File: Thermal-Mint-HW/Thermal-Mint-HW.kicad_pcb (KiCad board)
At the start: 4 copper layers, 90 x 54 mm, 36 parts, among them J1 Molex_5031821852, U1 ADS1220-VQFN, U2 ADS1220-VQFN, U3 ESP32-C3

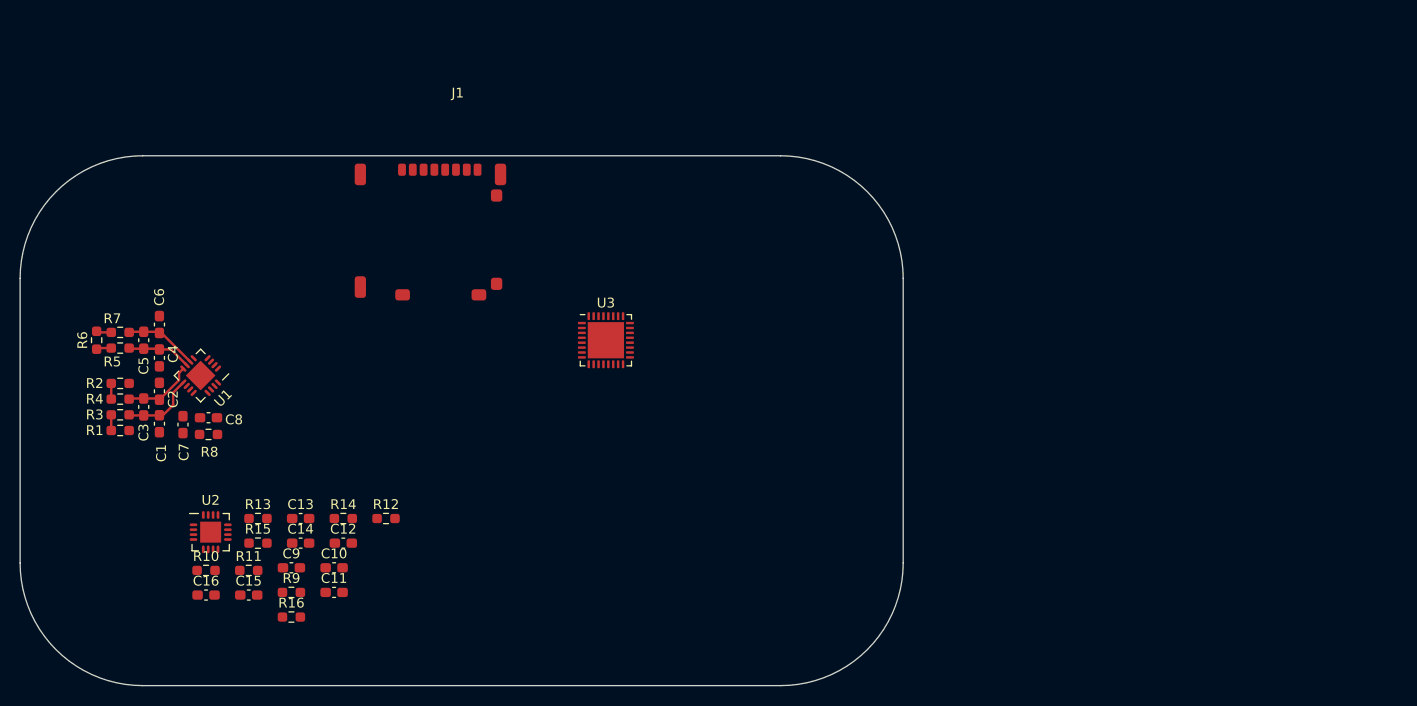
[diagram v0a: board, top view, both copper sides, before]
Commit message: WIP commit, Adding connectors and memory
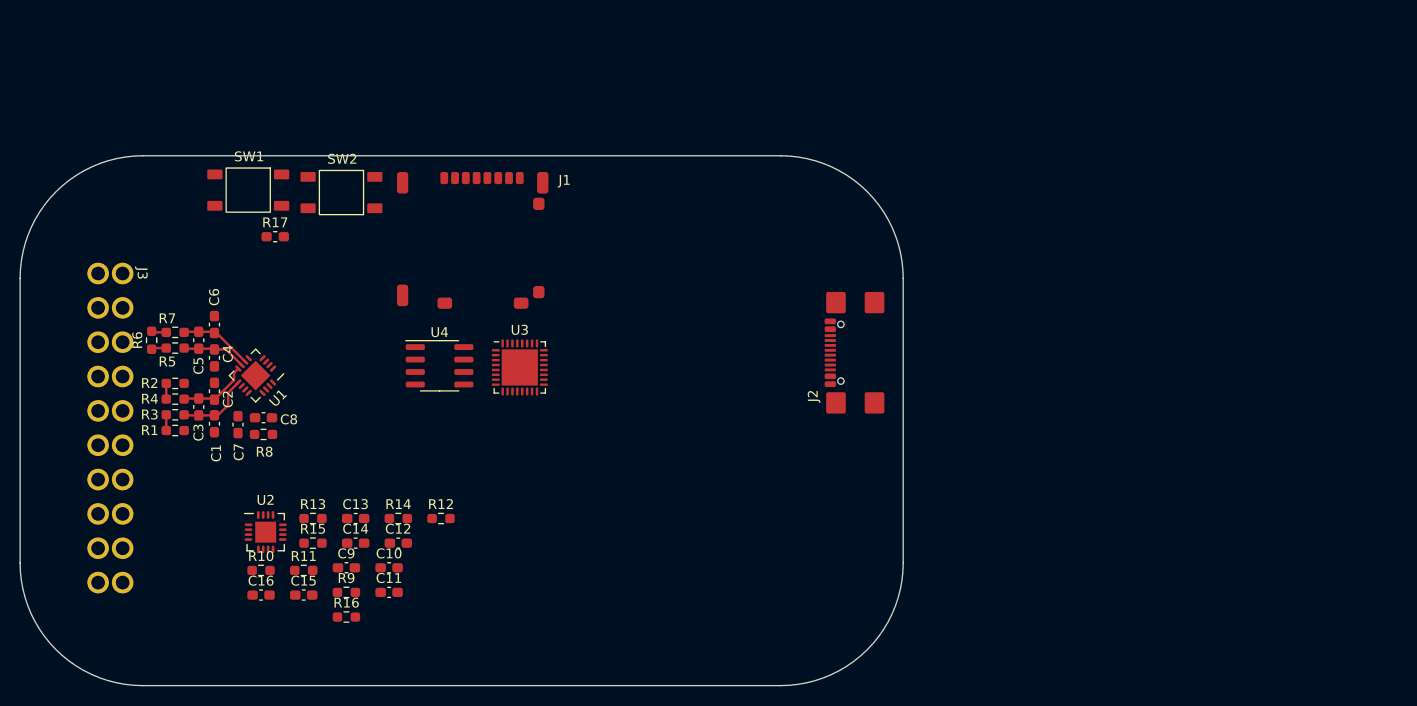
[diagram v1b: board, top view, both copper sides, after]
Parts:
- added J2: USB_C_Receptacle_USB2.0, ThermalMint:USB4110-GF-A, F.Cu at (144.6, 80.1)
- added J3: Conn_01x20_Male, ThermalMint:1786918_02_DMC, F.Cu at (72.5, 72.0)
- added R17: R, Resistor_SMD:R_0603_1608Metric_Pad1.05x0.95mm_HandSolder, F.Cu at (88.0, 68.2)
- added SW1: SW_SPST, ThermalMint:SW_SPST_PTS647, F.Cu at (85.2, 63.5)
- added SW2: SW_SPST, ThermalMint:SW_SPST_PTS647, F.Cu at (94.8, 63.8)
- added U4: AT25DL081-SSHN-T, Package_SO:SOIC-8_3.9x4.9mm_P1.27mm, F.Cu at (104.8, 81.4)
- J1: footprint CH:Molex_SDCard_5031821852 -> ThermalMint:Molex_SDCard_5031821852
- moved U3 9.20 mm to (112.9, 81.6)
- moved C10 5.61 mm to (99.6, 102.0)
- moved C11 5.61 mm to (99.6, 104.5)
- moved C12 5.61 mm to (100.5, 99.5)
- moved C15 5.61 mm to (90.9, 104.8)
- moved C3 5.61 mm to (80.2, 85.6)
- moved C5 5.61 mm to (80.2, 78.8)
- moved C7 5.61 mm to (84.2, 87.4)
- moved R11 5.61 mm to (90.9, 102.3)
- moved R13 5.61 mm to (91.8, 97.0)
- moved R14 5.61 mm to (100.5, 97.0)
- moved R15 5.61 mm to (91.8, 99.5)
- moved R6 5.61 mm to (75.4, 78.8)
- moved U2 5.61 mm to (87.0, 98.4)
- moved C1 5.61 mm to (81.8, 87.3)
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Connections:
- net /ADS1220_1/AIN0 renamed /ADC1AIN0
- net /ADS1220_1/AIN1 renamed /ADC1AIN1
- net /ADS1220_1/AIN2 renamed /ADC1AIN2
- net /ADS1220_1/RefIn renamed /ADC1REFIN
- net /ADS1220_1/nDRDY renamed Net-(R19-Pad1)
- net /ADS1220_2/AIN0 renamed /ADC2AIN0
- net /ADS1220_2/AIN1 renamed /ADC2AIN1
- net /ADS1220_2/RefIn renamed /ADC2REFIN
- net /ADS1220_2/nDRDY renamed Net-(R21-Pad1)
- net CS renamed /TM-ESP32/CS3
- net MISO renamed Net-(J1-Pad7)
- net RXD renamed /TM-ESP32/RXD
- net TXD renamed /TM-ESP32/TXD
- C16 pad 1: 3V3 -> +3V3
- C8 pad 1: 3V3 -> +3V3
- J1 pad 3: MOSI -> /ADS1220_1/DIN
- J1 pad 5: CLK -> /ADS1220_1/SCLK
- J1 pad 9: unconnected-(J1-Pad9) -> /TM-SDCard/cardDetect
- R16 pad 2: 3V3 -> +3V3
- R8 pad 2: 3V3 -> +3V3
- U1 pad 11: 3V3 -> +3V3
- U1 pad 13: /ADS1220_1/DOUT -> Net-(R18-Pad1)
- U1 pad 4: /ADS1220_1/AIN3 -> /ADC1AIN3
- U2 pad 11: 3V3 -> +3V3
- U2 pad 13: /ADS1220_1/DOUT -> Net-(R20-Pad1)
- U2 pad 4: /ADS1220_2/AIN3 -> /ADC3AIN3
- U2 pad 5: /ADS1220_2/AIN2 -> /ADC2AIN3
- U3 pad 1: unconnected-(U3-Pad1) -> /TM-ESP32/RF
- U3 pad 25: D- -> /TM-ESP32/D-
- U3 pad 26: D+ -> /TM-ESP32/D+
- U3 pad 33: unconnected-(U3-Pad33) -> GND

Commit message: Clean up of output circuits
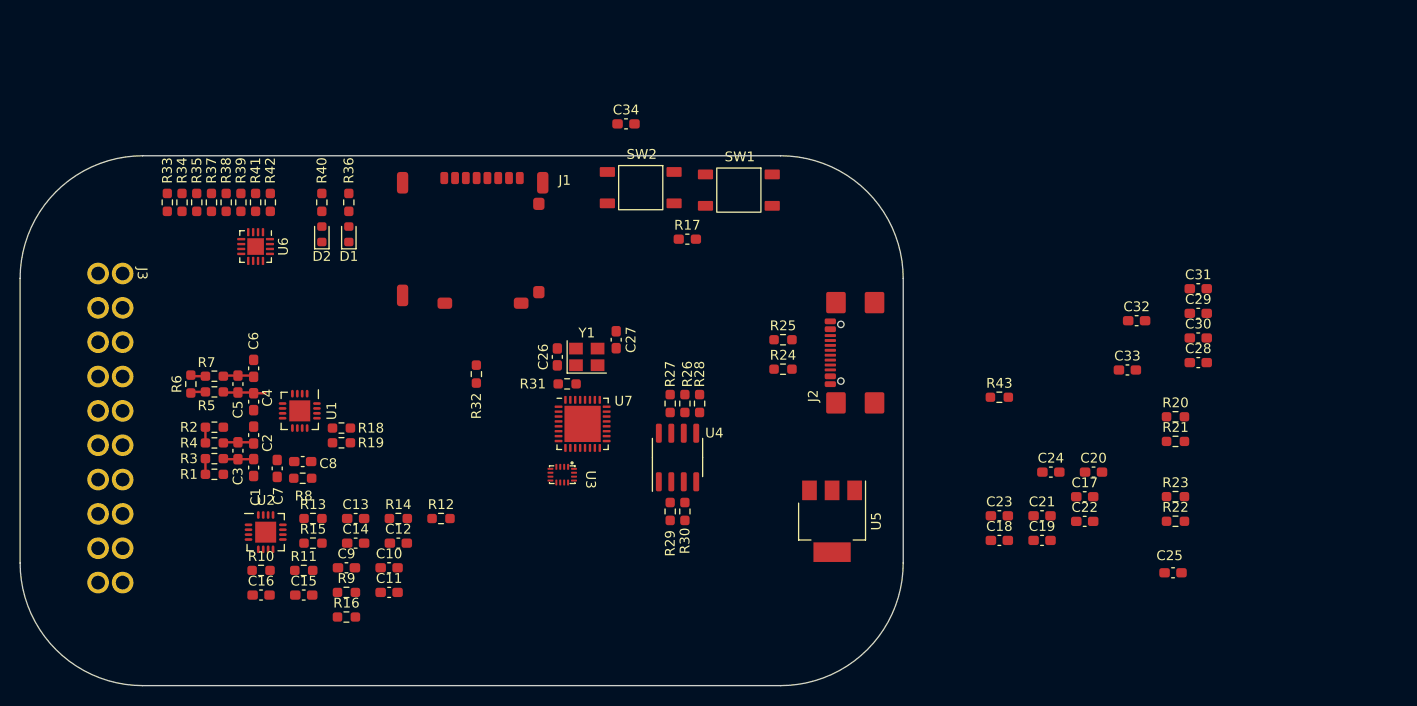
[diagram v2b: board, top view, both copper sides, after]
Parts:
- added C17: 470n, Capacitor_SMD:C_0603_1608Metric_Pad1.08x0.95mm_HandSolder, F.Cu at (170.5, 94.8)
- added C18: 470n, Capacitor_SMD:C_0603_1608Metric_Pad1.08x0.95mm_HandSolder, F.Cu at (161.8, 99.2)
- added C19: 470n, Capacitor_SMD:C_0603_1608Metric_Pad1.08x0.95mm_HandSolder, F.Cu at (166.2, 99.2)
- added C20: 470n, Capacitor_SMD:C_0603_1608Metric_Pad1.08x0.95mm_HandSolder, F.Cu at (171.4, 92.2)
- added C21: 470n, Capacitor_SMD:C_0603_1608Metric_Pad1.08x0.95mm_HandSolder, F.Cu at (166.2, 96.7)
- added C22: 470n, Capacitor_SMD:C_0603_1608Metric_Pad1.08x0.95mm_HandSolder, F.Cu at (170.5, 97.3)
- added C23: 470n, Capacitor_SMD:C_0603_1608Metric_Pad1.08x0.95mm_HandSolder, F.Cu at (161.8, 96.7)
- added C24: 470n, Capacitor_SMD:C_0603_1608Metric_Pad1.08x0.95mm_HandSolder, F.Cu at (167.1, 92.2)
- added C25: 470n, Capacitor_SMD:C_0603_1608Metric_Pad1.08x0.95mm_HandSolder, F.Cu at (179.5, 102.5)
- added C26: 15p, Capacitor_SMD:C_0603_1608Metric_Pad1.08x0.95mm_HandSolder, F.Cu at (116.8, 80.5)
- added C27: 15p, Capacitor_SMD:C_0603_1608Metric_Pad1.08x0.95mm_HandSolder, F.Cu at (122.8, 78.8)
- added C28: 470n, Capacitor_SMD:C_0603_1608Metric_Pad1.08x0.95mm_HandSolder, F.Cu at (182.1, 81.1)
- added C29: 470n, Capacitor_SMD:C_0603_1608Metric_Pad1.08x0.95mm_HandSolder, F.Cu at (182.1, 76.1)
- added C30: 470n, Capacitor_SMD:C_0603_1608Metric_Pad1.08x0.95mm_HandSolder, F.Cu at (182.1, 78.6)
- added C31: 470n, Capacitor_SMD:C_0603_1608Metric_Pad1.08x0.95mm_HandSolder, F.Cu at (182.1, 73.5)
- added C32: 470n, Capacitor_SMD:C_0603_1608Metric_Pad1.08x0.95mm_HandSolder, F.Cu at (175.8, 76.8)
- added C33: 470n, Capacitor_SMD:C_0603_1608Metric_Pad1.08x0.95mm_HandSolder, F.Cu at (174.8, 81.8)
- added C34: 470n, Capacitor_SMD:C_0603_1608Metric_Pad1.08x0.95mm_HandSolder, F.Cu at (123.8, 56.8)
- added D1: LED, LED_SMD:LED_0603_1608Metric, F.Cu at (95.5, 68.0)
- added D2: LED, LED_SMD:LED_0603_1608Metric, F.Cu at (92.8, 68.0)
- added R18: 24, Resistor_SMD:R_0603_1608Metric_Pad0.98x0.95mm_HandSolder, F.Cu at (94.8, 87.8)
- added R19: 24, Resistor_SMD:R_0603_1608Metric_Pad0.98x0.95mm_HandSolder, F.Cu at (94.8, 89.2)
- added R20: 24, Resistor_SMD:R_0603_1608Metric_Pad0.98x0.95mm_HandSolder, F.Cu at (179.8, 86.6)
- added R21: 24, Resistor_SMD:R_0603_1608Metric_Pad0.98x0.95mm_HandSolder, F.Cu at (179.8, 89.1)
- added R22: 24, Resistor_SMD:R_0603_1608Metric_Pad0.98x0.95mm_HandSolder, F.Cu at (179.8, 97.2)
- added R23: 10k, Resistor_SMD:R_0603_1608Metric_Pad0.98x0.95mm_HandSolder, F.Cu at (179.8, 94.7)
- added R24: 5.1k, Resistor_SMD:R_0603_1608Metric_Pad0.98x0.95mm_HandSolder, F.Cu at (139.8, 81.8)
- added R25: 5.1k, Resistor_SMD:R_0603_1608Metric_Pad0.98x0.95mm_HandSolder, F.Cu at (139.8, 78.8)
- added R26: R, Resistor_SMD:R_0603_1608Metric_Pad0.98x0.95mm_HandSolder, F.Cu at (129.8, 85.2)
- added R27: R, Resistor_SMD:R_0603_1608Metric_Pad0.98x0.95mm_HandSolder, F.Cu at (128.2, 85.2)
- added R28: R, Resistor_SMD:R_0603_1608Metric_Pad0.98x0.95mm_HandSolder, F.Cu at (131.2, 85.2)
- added R29: R, Resistor_SMD:R_0603_1608Metric_Pad0.98x0.95mm_HandSolder, F.Cu at (128.2, 96.2)
- added R30: R, Resistor_SMD:R_0603_1608Metric_Pad0.98x0.95mm_HandSolder, F.Cu at (129.8, 96.2)
- added R31: 0, Resistor_SMD:R_0603_1608Metric_Pad0.98x0.95mm_HandSolder, F.Cu at (117.8, 83.2)
- added R32: 10k, Resistor_SMD:R_0603_1608Metric_Pad0.98x0.95mm_HandSolder, F.Cu at (108.5, 82.2)
- added R33: 1k, Resistor_SMD:R_0603_1608Metric_Pad0.98x0.95mm_HandSolder, F.Cu at (77.0, 64.8)
- added R34: 1k, Resistor_SMD:R_0603_1608Metric_Pad0.98x0.95mm_HandSolder, F.Cu at (78.5, 64.8)
- added R35: 1k, Resistor_SMD:R_0603_1608Metric_Pad0.98x0.95mm_HandSolder, F.Cu at (80.0, 64.8)
- added R36: 1k, Resistor_SMD:R_0603_1608Metric_Pad0.98x0.95mm_HandSolder, F.Cu at (95.5, 64.8)
- added R37: 1k, Resistor_SMD:R_0603_1608Metric_Pad0.98x0.95mm_HandSolder, F.Cu at (81.5, 64.8)
- added R38: 1k, Resistor_SMD:R_0603_1608Metric_Pad0.98x0.95mm_HandSolder, F.Cu at (83.0, 64.8)
- added R39: 1k, Resistor_SMD:R_0603_1608Metric_Pad0.98x0.95mm_HandSolder, F.Cu at (84.5, 64.8)
- added R40: 1k, Resistor_SMD:R_0603_1608Metric_Pad0.98x0.95mm_HandSolder, F.Cu at (92.8, 64.8)
- added R41: 1k, Resistor_SMD:R_0603_1608Metric_Pad0.98x0.95mm_HandSolder, F.Cu at (86.0, 64.8)
- added R42: 1k, Resistor_SMD:R_0603_1608Metric_Pad0.98x0.95mm_HandSolder, F.Cu at (87.5, 64.8)
- added R43: 24, Resistor_SMD:R_0603_1608Metric_Pad0.98x0.95mm_HandSolder, F.Cu at (161.8, 84.6)
- added U3: SN74LVC138ARSVR, ThermalMint:UQFN16 - RSV0016A, F.Cu at (117.2, 92.5)
- added U5: NCP1117-3.3_SOT223, Package_TO_SOT_SMD:SOT-223-3_TabPin2, F.Cu at (144.8, 97.2)
- added U6: MAX7317ATE+, Package_DFN_QFN:QFN-16-1EP_3x3mm_P0.5mm_EP1.7x1.7mm, F.Cu at (86.0, 69.2)
- added Y1: FL4000157Z, Crystal:Crystal_SMD_3225-4Pin_3.2x2.5mm, F.Cu at (119.8, 80.5)
- J2: value USB_C_Receptacle_USB2.0 -> USB4110-GF-A
- R17: value R -> 10k
- SW1, SW2: value SW_SPST -> PTS647
- moved SW1 50.0 mm to (135.2, 63.5)
- moved R17 42.0 mm to (130.0, 68.5)
- moved SW2 30.5 mm to (125.2, 63.2)
- moved U4 26.0 mm to (129.0, 90.8), turned to 90 degrees
- moved U7 8.60 mm to (119.3, 87.3)
- moved C3 5.99 mm to (84.2, 90.1)
- moved C4 5.99 mm to (85.8, 85.1)
- moved C5 5.99 mm to (84.2, 83.3)
- moved R4 5.99 mm to (81.8, 89.3)
- moved R5 5.99 mm to (81.8, 84.1)
- moved R6 5.99 mm to (79.4, 83.3)
- moved C1 5.99 mm to (85.8, 91.8)
- moved C2 5.99 mm to (85.8, 88.5)
- moved C6 5.99 mm to (85.8, 81.7)
- moved C7 5.99 mm to (88.2, 91.9)
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- renumbered U3 to U7
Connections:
- net Net-(J2-PadA4) renamed /VBUS
- J2 pad A5: unconnected-(J2-PadA5) -> Net-(J2-PadA5)
- J2 pad B5: unconnected-(J2-PadB5) -> Net-(J2-PadB5)
- J3 pad 1: unconnected-(J3-Pad1) -> /GPO0
- J3 pad 11: unconnected-(J3-Pad11) -> GND
- J3 pad 12: unconnected-(J3-Pad12) -> GND
- J3 pad 13: unconnected-(J3-Pad13) -> GND
- J3 pad 14: unconnected-(J3-Pad14) -> GND
- J3 pad 15: unconnected-(J3-Pad15) -> /ADC1AIN2
- J3 pad 18: unconnected-(J3-Pad18) -> /ADC2AIN2
- J3 pad 19: /ADC3AIN3 -> /ADC2AIN3
- J3 pad 2: unconnected-(J3-Pad2) -> /GPO1
- J3 pad 3: unconnected-(J3-Pad3) -> /GPO2
- J3 pad 4: unconnected-(J3-Pad4) -> /GPO3
- R17 pad 1: unconnected-(R17-Pad1) -> +3V3
- R17 pad 2: Net-(R17-Pad2) -> Net-(C25-Pad1)
- SW1 pad 1: unconnected-(SW1-Pad1) -> Net-(U7-Pad15)
- SW1 pad 2: Net-(R17-Pad2) -> Net-(U7-Pad15)
- SW1 pad 3: (no net) -> GND
- SW1 pad 4: (no net) -> GND
- SW2 pad 1: unconnected-(SW2-Pad1) -> Net-(C25-Pad1)
- SW2 pad 2: unconnected-(SW2-Pad2) -> Net-(C25-Pad1)
- SW2 pad 3: (no net) -> GND
- SW2 pad 4: (no net) -> GND
- U4 pad 1: unconnected-(U4-Pad1) -> /TM-ESP32/SPICS0
- U4 pad 2: unconnected-(U4-Pad2) -> Net-(R29-Pad1)
- U4 pad 3: unconnected-(U4-Pad3) -> Net-(R30-Pad1)
- U4 pad 4: unconnected-(U4-Pad4) -> GND
- U4 pad 5: (no net) -> Net-(R28-Pad1)
- U4 pad 6: unconnected-(U4-Pad6) -> Net-(R26-Pad2)
- U4 pad 7: unconnected-(U4-Pad7) -> Net-(R27-Pad2)
- U4 pad 8: unconnected-(U4-Pad8) -> +3V3
- U7 pad 10: unconnected-(U3-Pad10) -> /TM-ESP32/DecoderA2
- U7 pad 11: unconnected-(U3-Pad11) -> +3V3
- U7 pad 12: unconnected-(U3-Pad12) -> /ADS1220_1/SCLK
- U7 pad 13: unconnected-(U3-Pad13) -> /ADS1220_1/DOUT
- U7 pad 14: unconnected-(U3-Pad14) -> /ADS1220_2/nDRDY
- U7 pad 15: unconnected-(U3-Pad15) -> Net-(U7-Pad15)
- U7 pad 16: unconnected-(U3-Pad16) -> /ADS1220_1/DIN
- U7 pad 17: unconnected-(U3-Pad17) -> +3V3
- U7 pad 18: unconnected-(U3-Pad18) -> /ADS1220_1/nDRDY
- U7 pad 19: unconnected-(U3-Pad19) -> /TM-ESP32/SPIHD
- U7 pad 2: unconnected-(U3-Pad2) -> +3V3
- U7 pad 20: unconnected-(U3-Pad20) -> /TM-ESP32/SPIWP
- U7 pad 21: unconnected-(U3-Pad21) -> /TM-ESP32/SPICS0
- U7 pad 22: unconnected-(U3-Pad22) -> /TM-ESP32/SPICLK
- U7 pad 23: unconnected-(U3-Pad23) -> /TM-ESP32/SPID
- U7 pad 24: unconnected-(U3-Pad24) -> /TM-ESP32/SPIQ
- U7 pad 29: unconnected-(U3-Pad29) -> /TM-ESP32/XTAL_N
- U7 pad 3: unconnected-(U3-Pad3) -> +3V3
- U7 pad 30: unconnected-(U3-Pad30) -> Net-(R31-Pad1)
- U7 pad 31: unconnected-(U3-Pad31) -> +3V3
- U7 pad 32: unconnected-(U3-Pad32) -> +3V3
- U7 pad 4: unconnected-(U3-Pad4) -> /TM-ESP32/XTAL_32k_P
- U7 pad 5: unconnected-(U3-Pad5) -> /TM-ESP32/XTAL_32k_N
- U7 pad 6: unconnected-(U3-Pad6) -> Net-(R32-Pad1)
- U7 pad 7: unconnected-(U3-Pad7) -> Net-(C25-Pad1)
- U7 pad 8: unconnected-(U3-Pad8) -> /TM-ESP32/DecoderA0
- U7 pad 9: unconnected-(U3-Pad9) -> /TM-ESP32/DecoderA1
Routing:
- net Net-(C1-Pad2): track 7.67 -> 3.47 mm
- net Net-(C2-Pad1): track 7.34 -> 3.17 mm
- net Net-(C5-Pad1): track 7.52 -> 3.38 mm
- net Net-(C4-Pad1): track 6.59 -> 4.33 mm

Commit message: Cleanup of Rev1 schematics for review
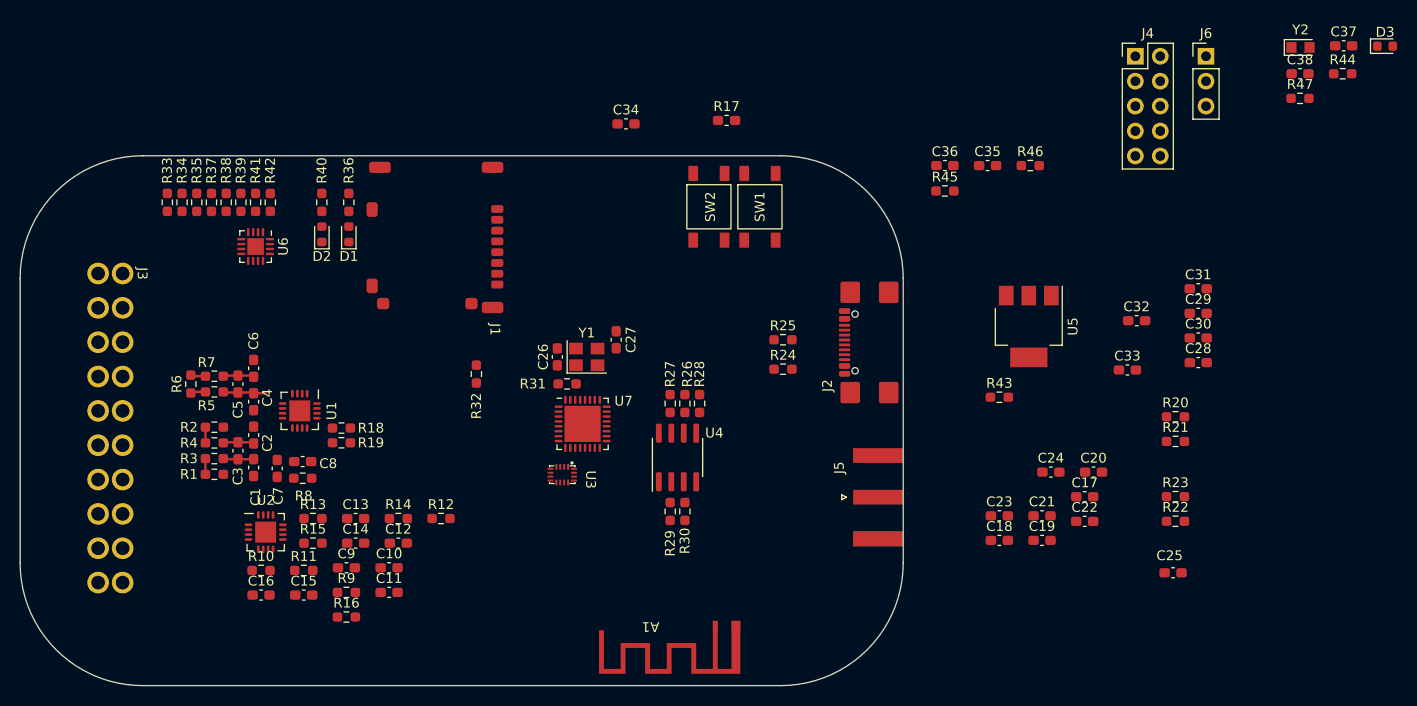
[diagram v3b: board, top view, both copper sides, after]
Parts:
- added A1: AntennaWithGround, ThermalMint:WifiAntenna, F.Cu at (135.4, 107.4)
- added C35: DNF, Capacitor_SMD:C_0603_1608Metric_Pad1.08x0.95mm_HandSolder, F.Cu at (160.6, 61.0)
- added C36: 1p, Capacitor_SMD:C_0603_1608Metric_Pad1.08x0.95mm_HandSolder, F.Cu at (156.2, 61.0)
- added C37: DNF, Capacitor_SMD:C_0603_1608Metric_Pad1.08x0.95mm_HandSolder, F.Cu at (196.9, 48.8)
- added C38: DNF, Capacitor_SMD:C_0603_1608Metric_Pad1.08x0.95mm_HandSolder, F.Cu at (192.4, 51.6)
- added D3: LED, LED_SMD:LED_0603_1608Metric, F.Cu at (201.1, 48.8)
- added J4: Conn_01x12_Male, Connector_PinHeader_2.54mm:PinHeader_2x05_P2.54mm_Vertical, F.Cu at (175.7, 49.9)
- added J5: Conn_Coaxial, Connector_Coaxial:SMA_Amphenol_132289_EdgeMount, F.Cu at (149.4, 94.8)
- added J6: Conn_01x03_Female, Connector_PinHeader_2.54mm:PinHeader_1x03_P2.54mm_Vertical, F.Cu at (182.9, 49.9)
- added R44: 1k, Resistor_SMD:R_0603_1608Metric_Pad0.98x0.95mm_HandSolder, F.Cu at (196.8, 51.6)
- added R45: DNF, Resistor_SMD:R_0603_1608Metric_Pad0.98x0.95mm_HandSolder, F.Cu at (156.2, 63.6)
- added R46: 0, Resistor_SMD:R_0603_1608Metric_Pad0.98x0.95mm_HandSolder, F.Cu at (164.9, 61.0)
- added R47: DNF, Resistor_SMD:R_0603_1608Metric_Pad0.98x0.95mm_HandSolder, F.Cu at (192.4, 54.1)
- added Y2: CM8V-T1A-32.768KHZ-12.5PF-20PPM-TA-QA, Crystal:Crystal_SMD_TXC_9HT11-2Pin_2.0x1.2mm_HandSoldering, F.Cu at (192.5, 49.0)
- R1, R10, R2, R9: value 10k -> DNF
- R26, R27, R28, R29, R30: value R -> 24
- moved U5 28.2 mm to (164.8, 77.4)
- moved R17 12.7 mm to (134.0, 56.4)
- moved J1 10.9 mm to (111.2, 60.6), turned to -90 degrees
- moved SW2 7.22 mm to (132.2, 65.2), turned to 90 degrees
- moved SW1 2.74 mm to (137.4, 65.2), turned to 90 degrees
- moved J2 1.79 mm to (146.0, 79.0)
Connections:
- net /ADS1220_1/DIN renamed /DOUT
- net /ADS1220_1/DOUT renamed /DIN
- net /ADS1220_1/SCLK renamed /SCLK
- net /ADS1220_1/nDRDY renamed /nDRDY1
- net /ADS1220_2/nDRDY renamed /nDRDY2
- net /GPO0 renamed /GPIO0
- net /GPO1 renamed /GPIO1
- net /GPO2 renamed /GPIO2
- net /GPO3 renamed /GPIO3
- net /TM-GPO/GPO4 renamed /GPIO4
- net /TM-GPO/GPO5 renamed /GPIO5
- net /TM-GPO/GPO6 renamed /GPIO6
- C28 pad 1: /VBUS -> +5V
- C29 pad 1: /VBUS -> +5V
- J1 pad 2: /TM-ESP32/CS3 -> /CS3
- J1 pad 9: /TM-SDCard/cardDetect -> /GPIO7
- J2 pad A4: /VBUS -> +5V
- J2 pad A9: /VBUS -> +5V
- J2 pad B4: /VBUS -> +5V
- J2 pad B9: /VBUS -> +5V
- J3 pad 15: /ADC1AIN2 -> GND
- J3 pad 16: /ADC1AIN3 -> /ADC1AIN2
- J3 pad 18: /ADC2AIN2 -> GND
- J3 pad 19: /ADC2AIN3 -> /ADC2AIN2
- R23 pad 2: /TM-SDCard/cardDetect -> /GPIO7
- U1 pad 16: /ADS1220_1/CS -> /CS1
- U2 pad 16: /ADS1220_2/CS -> /CS2
- U3 pad 10: /TM-ESP32/CS6 -> /CS5
- U3 pad 11: /TM-ESP32/CS5 -> /CS4
- U3 pad 12: /TM-ESP32/CS4 -> /CS3
- U3 pad 13: /TM-ESP32/CS3 -> /CS2
- U3 pad 14: /ADS1220_2/CS -> /CS1
- U3 pad 15: /ADS1220_1/CS -> Net-(D3-Pad1)
- U3 pad 6: unconnected-(U3-Pad6) -> +3V3
- U3 pad 7: /TM-ESP32/CS8 -> /CS7
- U3 pad 9: /TM-ESP32/CS7 -> /CS6
- U5 pad 3: /VBUS -> +5V
- U6 pad 16: /TM-ESP32/CS4 -> /CS4
- U6 pad 9: /TM-GPO/GPO7 -> /GPIO7
